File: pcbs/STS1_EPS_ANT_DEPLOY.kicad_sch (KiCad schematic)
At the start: 4 parts, among them Q21 SI7272DP-T1-GE3, Q22 SI7272DP-T1-GE3

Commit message: Fixed some warnings and errors.
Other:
- moved on the sheet: Q21B, Q22B, TP24, TP25

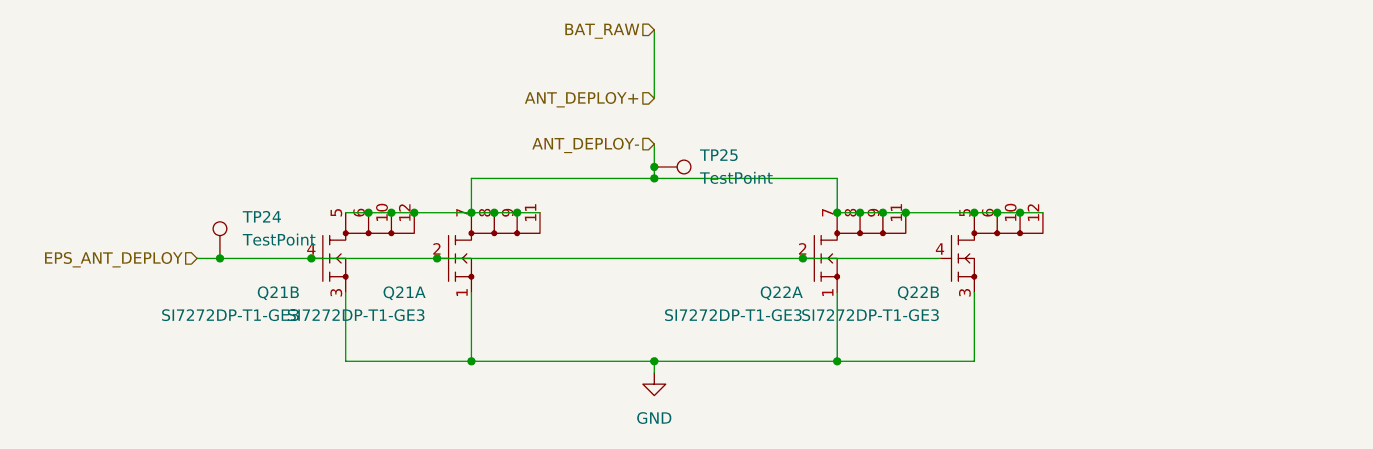
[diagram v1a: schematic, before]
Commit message: Fixed warnings and errors.
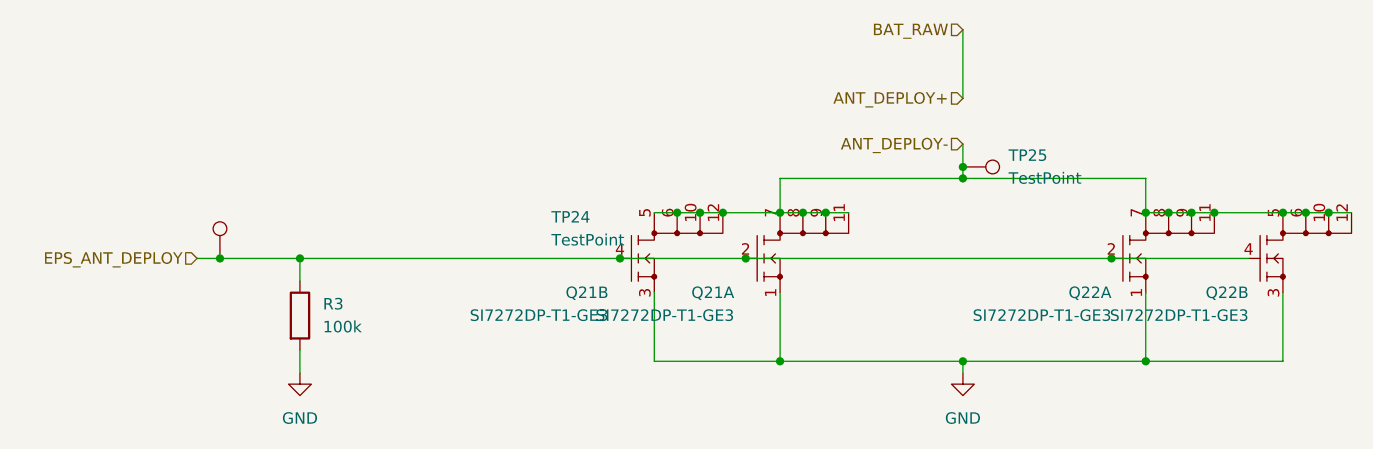
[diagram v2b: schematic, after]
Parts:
- added R3: 100k, Capacitor_SMD:C_0805_2012Metric, symbol Device:R
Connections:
- net EPS_ANT_DEPLOY: now also R3.1
- net GND: now also R3.2
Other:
- moved on the sheet: Q21A, Q21B, Q22A, Q22B, TP25

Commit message: Added more part numbers.
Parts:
- R3: footprint Capacitor_SMD:C_0805_2012Metric -> Resistor_SMD:R_0805_2012Metric; Part Nr. (none) -> TNPW0805100KFEEA
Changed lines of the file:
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@@
+			)
+		)
+		(property "Part Nr." ""
+			(at 134.62 99.06 0)
+			(effects
+				(font
+					(size 1.27 1.27)
+				)
+				(hide yes)
 			)
 		)
@@
 			)
 		)
+		(property "Part Nr." ""
+			(at 149.86 99.06 0)
+			(effects
+				(font
+					(size 1.27 1.27)
+				)
+				(hide yes)
+			)
+		)
 		(pin "1"
 		)
@@
 				)
 				(justify left)
+				(hide yes)
+			)
+		)
+		(property "Part Nr." ""
+			(at 93.98 99.06 0)
+			(effects
+				(font
+					(size 1.27 1.27)
+				)
 				(hide yes)
 			)
@@
 			)
 		)
+		(property "Part Nr." ""
+			(at 80.01 99.06 0)
+			(effects
+				(font
+					(size 1.27 1.27)
+				)
+				(hide yes)
+			)
+		)
 		(pin "1"
 		)
@@
 			)
 		)
+		(property "Part Nr." ""
+			(at 118.11 88.9 0)
+			(effects
+				(font
+					(size 1.27 1.27)
+				)
+				(hide yes)
+			)
+		)
 		(pin "1"
 		)
@@
 		)
 		(property "Description" ""
+			(at 35.56 99.06 0)
+			(effects
+				(font
+					(size 1.27 1.27)
+				)
+				(hide yes)
+			)
+		)
+		(property "Part Nr." ""
 			(at 35.56 99.06 0)
 			(effects
@@
 			)
 		)
-		(property "Footprint" "Capacitor_SMD:C_0805_2012Metric"
+		(property "Footprint" "Resistor_SMD:R_0805_2012Metric"
 			(at 42.672 105.41 90)
 			(effects
@@
 			(at 44.45 105.41 0)
 			(effects
+				(font
+					(size 1.27 1.27)
+				)
+				(hide yes)
+			)
+		)
+		(property "Part Nr." "TNPW0805100KFEEA"
+			(at 44.45 105.41 0)
+			(effects
